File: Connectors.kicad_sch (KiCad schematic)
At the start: 16 parts, among them J16 USB_A_Stacked, J23 HR911130A, J24 HR911130A, U1 TPS2065CDBV

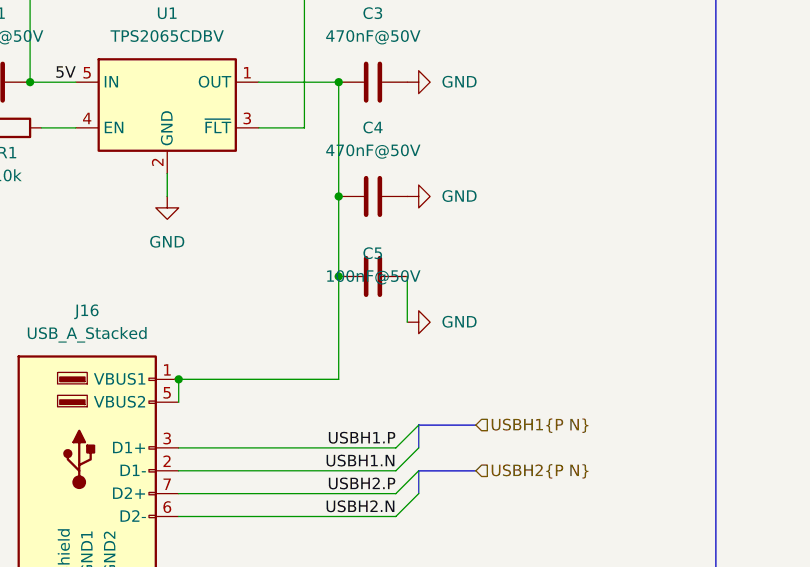
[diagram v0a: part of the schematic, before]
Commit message: Add RoHS Compliance Summary
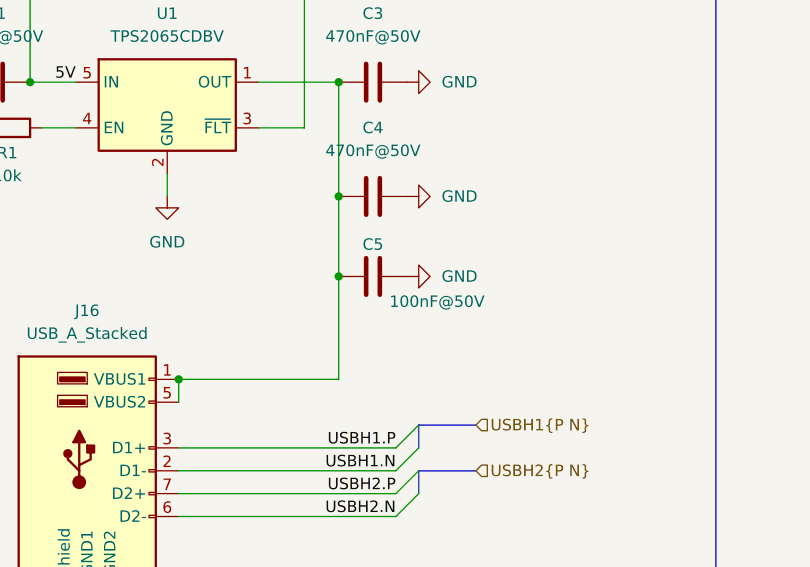
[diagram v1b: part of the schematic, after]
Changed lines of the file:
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@@
-	(wire
-		(pts
-			(xy 109.22 173.99) (xy 109.22 168.91)
-		)
-		(stroke
-			(width 0)
-			(type default)
-		)
-	)
 	(wire
 		(pts
@@
 			)
 		)
+		(property "MPN" ""
+			(at 254 137.16 0)
+			(effects
+				(font
+					(size 1.27 1.27)
+				)
+			)
+		)
 		(pin "4"
 		)
@@
 			)
 		)
+		(property "MPN" ""
+			(at 64.77 152.4 0)
+			(effects
+				(font
+					(size 1.27 1.27)
+				)
+			)
+		)
 		(pin "2"
 		)
@@
 			)
 		)
+		(property "MPN" ""
+			(at 105.41 160.02 0)
+			(effects
+				(font
+					(size 1.27 1.27)
+				)
+			)
+		)
 		(pin "1"
 		)
@@
 			)
 		)
+		(property "MPN" ""
+			(at 105.41 147.32 0)
+			(effects
+				(font
+					(size 1.27 1.27)
+				)
+			)
+		)
 		(pin "1"
 		)
@@
 		(dnp no)
 		(property "Reference" "C5"
-			(at 105.41 166.37 90)
+			(at 105.41 165.354 90)
 			(effects
 				(font
@@
 		)
 		(property "Value" "100nF@50V"
-			(at 105.41 168.91 90)
+			(at 112.522 171.704 90)
 			(effects
 				(font
@@
 				)
 				(hide yes)
+			)
+		)
+		(property "MPN" ""
+			(at 105.41 168.91 0)
+			(effects
+				(font
+					(size 1.27 1.27)
+				)
 			)
 		)
@@
 				)
 				(hide yes)
+			)
+		)
+		(property "MPN" ""
+			(at 82.55 149.86 0)
+			(effects
+				(font
+					(size 1.27 1.27)
+				)
 			)
 		)
@@
 			)
 		)
+		(property "MPN" ""
+			(at 63.5 147.32 0)
+			(effects
+				(font
+					(size 1.27 1.27)
+				)
+			)
+		)
 		(pin "2"
 		)
@@
 				)
 				(hide yes)
+			)
+		)
+		(property "MPN" ""
+			(at 227.33 240.03 0)
+			(effects
+				(font
+					(size 1.27 1.27)
+				)
 			)
 		)
@@
 			)
 		)
+		(property "MPN" ""
+			(at 227.33 139.7 0)
+			(effects
+				(font
+					(size 1.27 1.27)
+				)
+			)
+		)
 		(pin "2"
 		)
@@
 			)
 		)
+		(property "MPN" ""
+			(at 73.66 190.5 0)
+			(effects
+				(font
+					(size 1.27 1.27)
+				)
+			)
+		)
 		(pin "3"
 		)
@@
 				)
 				(hide yes)
+			)
+		)
+		(property "MPN" ""
+			(at 231.14 199.39 0)
+			(effects
+				(font
+					(size 1.27 1.27)
+				)
 			)
 		)
@@
 			)
 		)
+		(property "MPN" ""
+			(at 82.55 135.89 0)
+			(effects
+				(font
+					(size 1.27 1.27)
+				)
+			)
+		)
 		(pin "2"
 		)
@@
 			)
 		)
+		(property "MPN" ""
+			(at 231.14 111.76 0)
+			(effects
+				(font
+					(size 1.27 1.27)
+				)
+			)
+		)
 		(pin "2"
 		)
@@
 				)
 				(hide yes)
+			)
+		)
+		(property "MPN" ""
+			(at 227.33 152.4 0)
+			(effects
+				(font
+					(size 1.27 1.27)
+				)
 			)
 		)
@@
 	(symbol
 		(lib_id "power:GND")
-		(at 109.22 173.99 90)
+		(at 109.22 168.91 90)
 		(mirror x)
 		(unit 1)
@@
 		(fields_autoplaced yes)
 		(property "Reference" "#PWR016"
-			(at 115.57 173.99 0)
+			(at 115.57 168.91 0)
 			(effects
 				(font
@@
 		)
 		(property "Value" "GND"
-			(at 113.03 173.9899 90)
+			(at 113.03 168.9099 90)
 			(effects
 				(font
@@
 		)
 		(property "Footprint" ""
-			(at 109.22 173.99 0)
+			(at 109.22 168.91 0)
 			(effects
 				(font
@@
 		)
 		(property "Datasheet" ""
-			(at 109.22 173.99 0)
+			(at 109.22 168.91 0)
 			(effects
 				(font
@@
 		)
 		(property "Description" "Power symbol creates a global label with name \"GND\" , ground"
-			(at 109.22 173.99 0)
+			(at 109.22 168.91 0)
 			(effects
 				(font
@@
 			)
 		)
+		(property "MPN" ""
+			(at 227.33 227.33 0)
+			(effects
+				(font
+					(size 1.27 1.27)
+				)
+			)
+		)
 		(pin "2"
 		)
@@
 			)
 		)
+		(property "MPN" ""
+			(at 254 224.79 0)
+			(effects
+				(font
+					(size 1.27 1.27)
+				)
+			)
+		)

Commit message: v0.3 prototype
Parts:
- C1, C22, C23, C5: value 100nF@50V -> 100nF
- J16: footprint Connector_USB:USB_A_Wuerth_61400826021_Horizontal_Stacked -> easyeda2kicad:USB-A-TH_USB-269-BRW; FT Rotation Offset 180 -> 0
- J23, J24: Availability (none) -> In Stock; Check_prices (none) -> https://www.snapeda.com/parts/HR911130A/HanRun/view-part/?r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; MANUFACTURER (none) -> HanRun; MAXIMUM_PACKAGE_HEIGHT (none) -> 13.75 mm; PARTREV (none) -> A; Package (none) -> None; Price (none) -> None; STANDARD (none) -> Manufacturer Recommendations; SnapEDA_Link (none) -> https://www.snapeda.com/parts/HR911130A/HanRun/view-part/?r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

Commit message: BOM optimization
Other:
- title: OpenMower SABO Mainboard for Series I & II -> OpenMower SABO Carrierboard for Series I & II
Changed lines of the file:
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@@
 	(paper "A3")
 	(title_block
-		(title "OpenMower SABO Mainboard for Series I & II")
-		(date "2025-10-05")
-		(rev "v0.3")
+		(title "OpenMower SABO Carrierboard for Series I & II")
+		(date "2025-10-12")
+		(rev "v0.4")
 		(company "Apeheanger <joerg@ebeling.ws> for OpenMower")
 		(comment 1 "This design is licensed under CC BY-NC 4.0")
@@
 			)
 		)
-		(property "Description" "Unpolarized capacitor"
+		(property "Description" "50V 100nF X7R ±10% 0402 Multilayer Ceramic Capacitors MLCC"
 			(at 105.41 168.91 0)
 			(effects
@@
 			)
 		)
-		(property "Description" "Unpolarized capacitor"
+		(property "Description" "50V 100nF X7R ±10% 0402 Multilayer Ceramic Capacitors MLCC"
 			(at 63.5 147.32 0)
 			(effects
@@
 			)
 		)
-		(property "Description" "Unpolarized capacitor"
+		(property "Description" "50V 100nF X7R ±10% 0402 Multilayer Ceramic Capacitors MLCC"
 			(at 231.14 199.39 0)
 			(effects
@@
 			)
 		)
-		(property "Description" "Unpolarized capacitor"
+		(property "Description" "50V 100nF X7R ±10% 0402 Multilayer Ceramic Capacitors MLCC"
 			(at 231.14 111.76 0)
 			(effects

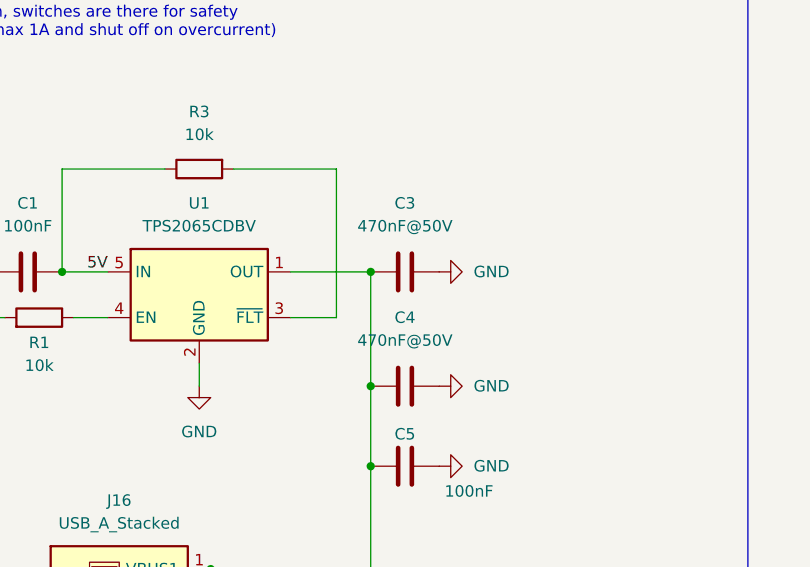
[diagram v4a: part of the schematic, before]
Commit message: BOM optimization
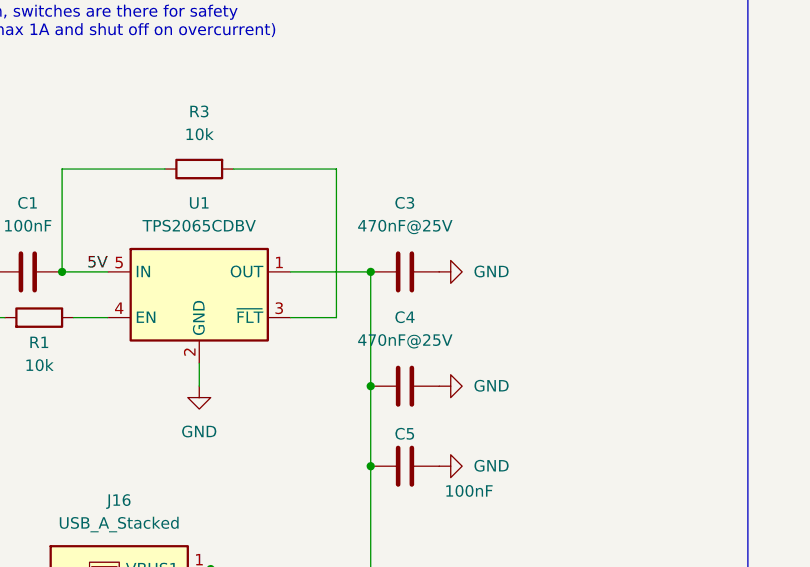
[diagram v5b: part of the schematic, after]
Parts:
- C3, C4: value 470nF@50V -> 470nF@25V; footprint Capacitor_SMD:C_0805_2012Metric -> Capacitor_SMD:C_0603_1608Metric; JLC C13967 -> C1623

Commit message: Add latest findings
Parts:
- removed C22: 100nF, Capacitor_SMD:C_0402_1005Metric, symbol Device:C
- removed J23: HR911130A, local_Connectors:HR911130A, symbol local_Connectors:HR911130A
- removed R11, R12: 300, Resistor_SMD:R_0603_1608Metric, symbol Device:R

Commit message: Prepare for next production - Slightly adapt part selection - Add TC2050 holes
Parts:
- C1, C23, C5: JLC C307331 -> (none); LCSC Part # (none) -> C307331
- C3, C4: JLC C1623 -> (none); LCSC Part # (none) -> C1623
- J16: JLC C720548 -> (none); LCSC Part # (none) -> C720548
- J24: JLC C54408 -> (none); LCSC Part # (none) -> C54408; MFPN (none) -> HR911130A; MP HR911130A -> (none)
- R1, R3: JLC C25744 -> (none); LCSC Part # (none) -> C25744
- R13, R14: JLC C23025 -> (none); LCSC Part # (none) -> C23025
- U1: JLC C353882 -> (none); LCSC Part # (none) -> C353882
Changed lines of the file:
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@@
-			)
-		)
-		(property "JLC" "C1623"
-			(at 105.41 160.02 0)
-			(effects
-				(font
-					(size 1.27 1.27)
-				)
-				(hide yes)
-			)
-		)
-		(property "MPN" ""
-			(at 105.41 160.02 0)
-			(effects
-				(font
-					(size 1.27 1.27)
-				)
 			)
 		)
@@
 			)
 		)
-		(property "LCSC" ""
+		(property "LCSC Part #" "C1623"
 			(at 105.41 160.02 90)
 			(effects
@@
 			)
 		)
-		(property "JLC" "C25744"
-			(at 64.77 152.4 0)
-			(effects
-				(font
-					(size 1.27 1.27)
-				)
-				(hide yes)
-			)
-		)
-		(property "MPN" ""
-			(at 64.77 152.4 0)
-			(effects
-				(font
-					(size 1.27 1.27)
-				)
-			)
-		)
 		(property "Alternative" ""
 			(at 64.77 152.4 90)
@@
 			)
 		)
-		(property "LCSC" ""
+		(property "LCSC Part #" "C25744"
 			(at 64.77 152.4 90)
 			(effects
@@
 			)
 		)
-		(property "JLC" "C307331"
-			(at 105.41 168.91 0)
-			(effects
-				(font
-					(size 1.27 1.27)
-				)
-				(hide yes)
-			)
-		)
-		(property "MPN" ""
-			(at 105.41 168.91 0)
-			(effects
-				(font
-					(size 1.27 1.27)
-				)
-			)
-		)
 		(property "Alternative" ""
 			(at 105.41 168.91 90)
@@
 			)
 		)
-		(property "LCSC" ""
+		(property "LCSC Part #" "C307331"
 			(at 105.41 168.91 90)
 			(effects
@@
 			)
 		)
-		(property "JLC" "C353882"
-			(at 82.55 149.86 0)
-			(effects
-				(font
-					(size 1.27 1.27)
-				)
-				(hide yes)
-			)
-		)
 		(property "FT Rotation Offset" "90"
 			(at 82.55 149.86 0)
@@
 			)
 		)
-		(property "MPN" ""
-			(at 82.55 149.86 0)
-			(effects
-				(font
-					(size 1.27 1.27)
-				)
-			)
-		)
 		(property "Alternative" ""
 			(at 82.55 149.86 0)
@@
 			)
 		)
-		(property "LCSC" ""
+		(property "LCSC Part #" "C353882"
 			(at 82.55 149.86 0)
 			(effects
@@
 			)
 		)
-		(property "JLC" "C307331"
-			(at 63.5 147.32 0)
-			(effects
-				(font
-					(size 1.27 1.27)
-				)
-				(hide yes)
-			)
-		)
-		(property "MPN" ""
-			(at 63.5 147.32 0)
-			(effects
-				(font
-					(size 1.27 1.27)
-				)
-			)
-		)
 		(property "Alternative" ""
 			(at 63.5 147.32 90)
@@
 			)
 		)
-		(property "LCSC" ""
+		(property "LCSC Part #" "C307331"
 			(at 63.5 147.32 90)
 			(effects
@@
 			)
 		)
-		(property "JLC" "C23025"
-			(at 227.33 240.03 0)
-			(effects
-				(font
-					(size 1.27 1.27)
-				)
-				(hide yes)
-			)
-		)
-		(property "MPN" ""
-			(at 227.33 240.03 0)
-			(effects
-				(font
-					(size 1.27 1.27)
-				)
-			)
-		)
 		(property "Alternative" ""
 			(at 227.33 240.03 90)
@@
 			)
 		)
-		(property "LCSC" ""
+		(property "LCSC Part #" "C23025"
 			(at 227.33 240.03 90)
 			(effects
@@
 			)
 		)
-		(property "JLC" "C1623"
-			(at 105.41 147.32 0)
-			(effects
-				(font
-					(size 1.27 1.27)
-				)
-				(hide yes)
-			)
-		)
-		(property "MPN" ""
-			(at 105.41 147.32 0)
-			(effects
-				(font
-					(size 1.27 1.27)
-				)
-			)
-		)
 		(property "Alternative" ""
 			(at 105.41 147.32 90)
@@
 			)
 		)
-		(property "LCSC" ""
+		(property "LCSC Part #" "C1623"
 			(at 105.41 147.32 90)
 			(effects
@@
 			)
 		)
-		(property "JLC" "C720548"
-			(at 73.66 190.5 0)
-			(effects
-				(font
-					(size 1.27 1.27)
-				)
-				(hide yes)
-			)
-		)
 		(property "FT Rotation Offset" "0"
 			(at 73.66 190.5 0)
@@
 			)
 		)
-		(property "MPN" ""
-			(at 73.66 190.5 0)
-			(effects
-				(font
-					(size 1.27 1.27)
-				)
-			)
-		)
 		(property "Alternative" ""
 			(at 73.66 190.5 0)
@@
 			)
 		)
-		(property "LCSC" ""
+		(property "LCSC Part #" "C720548"
 			(at 73.66 190.5 0)
 			(effects
@@
 			)
 		)
-		(property "JLC" "C307331"
-			(at 231.14 199.39 0)
-			(effects
-				(font
-					(size 1.27 1.27)
-				)
-				(hide yes)
-			)
-		)
-		(property "MPN" ""
-			(at 231.14 199.39 0)
-			(effects
-				(font
-					(size 1.27 1.27)
-				)
-			)
-		)
 		(property "Alternative" ""
 			(at 231.14 199.39 90)
@@
 			)
 		)
-		(property "LCSC" ""
+		(property "LCSC Part #" "C307331"
 			(at 231.14 199.39 90)
 			(effects
@@
 			)
 		)
-		(property "JLC" "C25744"
-			(at 82.55 135.89 0)
-			(effects
-				(font
-					(size 1.27 1.27)
-				)
-				(hide yes)
-			)
-		)
-		(property "MPN" ""
-			(at 82.55 135.89 0)
-			(effects
-				(font
-					(size 1.27 1.27)
-				)
-			)
-		)
 		(property "Alternative" ""
 			(at 82.55 135.89 90)
@@
 			)
 		)
-		(property "LCSC" ""
+		(property "LCSC Part #" "C25744"
 			(at 82.55 135.89 90)
 			(effects
@@
 			)
 		)
-		(property "JLC" "C23025"
-			(at 227.33 227.33 0)
-			(effects
-				(font
-					(size 1.27 1.27)
-				)
-				(hide yes)
-			)
-		)
-		(property "MPN" ""
-			(at 227.33 227.33 0)
-			(effects
-				(font
-					(size 1.27 1.27)
-				)
-			)
-		)
 		(property "Alternative" ""
 			(at 227.33 227.33 90)
@@
 			)
 		)
-		(property "LCSC" ""
+		(property "LCSC Part #" "C23025"
 			(at 227.33 227.33 90)
 			(effects
@@
 			)
 		)
-		(property "MP" "HR911130A"
-			(at 254 224.79 0)
-			(effects
-				(font
-					(size 1.27 1.27)
-				)
-				(justify bottom)
-				(hide yes)
-			)
-		)
-		(property "JLC" "C54408"
-			(at 254 224.79 0)
-			(effects
-				(font
-					(size 1.27 1.27)
-				)
-				(hide yes)
-			)
-		)
-		(property "MPN" ""
-			(at 254 224.79 0)
-			(effects
-				(font
-					(size 1.27 1.27)
-				)
-			)
-		)
 		(property "MAXIMUM_PACKAGE_HEIGHT" "13.75 mm"
 			(at 254 224.79 0)
@@
 			)
 		)
-		(property "LCSC" ""
+		(property "LCSC Part #" "C54408"
 			(at 254 224.79 0)
 			(effects
+				(font
+					(size 1.27 1.27)
+				)
+				(hide yes)
+			)
+		)
+		(property "MFPN" "HR911130A"
+			(at 254 224.79 0)
+			(effects

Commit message: Next proto prep
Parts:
- U1: value TPS2065CDBV -> TPS2065CDBVR
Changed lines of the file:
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@@
 			)
 		)
-		(property "Value" "TPS2065CDBV"
+		(property "Value" "TPS2065CDBVR"
 			(at 82.55 142.24 0)
 			(effects
